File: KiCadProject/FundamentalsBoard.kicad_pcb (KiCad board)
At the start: 2 copper layers, 62 parts, among them P1 CONN_02X02, P10 CONN_02X02, P11 CONN_01X03, P12 CONN_01X03, P2 CONN_02X02, P3 USB_OTG, P4 CONN_02X02, P5 CONN_01X03, P6 CONN_02X02, P7 CONN_02X02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

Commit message: Initial layout
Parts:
- P1, P10, P2, P4, P6, P7, P8: footprint Pin_Headers:Pin_Header_Straight_2x02 -> TylerCustom:Pin_Header_Straight_2x02
- RV1, RV10, RV2, RV3, RV4, RV5, RV6, RV7, RV8, RV9: footprint SMD_Packages:POT_SMD -> TylerCustom:ST-4
- moved P3 116.6 mm to (83.2, 130.2), turned to 270 degrees
- moved RV9 90.9 mm to (176.5, 134.0), turned to 90 degrees
- moved RV10 76.9 mm to (152.4, 134.0), turned to 90 degrees
- moved P2 66.8 mm to (178.4, 112.4)
- moved C1 64.0 mm to (88.3, 130.2), turned to 90 degrees
- moved C2 62.4 mm to (90.2, 130.2), turned to 90 degrees
- moved RV3 59.2 mm to (97.2, 120.7), turned to 90 degrees
- moved P9 55.3 mm to (120.7, 131.4)
- moved C3 54.4 mm to (91.4, 111.1), turned to 180 degrees
- moved R8 51.9 mm to (94.6, 113.7), turned to 270 degrees
- moved R17 51.1 mm to (94.6, 89.5), turned to 270 degrees
- moved R7 50.9 mm to (94.6, 109.2), turned to 270 degrees
- moved U5 48.3 mm to (97.8, 88.3)
- moved R12 48.2 mm to (99.1, 115.6)
- moved Q1 47.3 mm to (99.1, 112.4), turned to 180 degrees
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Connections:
- C1 pad 2: CMirror_p -> VCC
- C2 pad 2: CMirror_p -> VCC
- P3 pad 1: CMirror_p -> VCC
- P6 pad 1: CMirror_p -> VCC
- P6 pad 2: CMirror_p -> VCC
- R10 pad 1: CMirror_p -> VCC
- R11 pad 1: Net-(R11-Pad1) -> VCC
- R7 pad 1: Net-(R11-Pad1) -> VCC
- RV1 pad 1: CMirror_p -> VCC
- RV5 pad 2: CMirror_p -> VCC
- U1 pad 5: CMirror_p -> VCC
- U2 pad 5: CMirror_p -> VCC
- U3 pad 5: CMirror_p -> VCC
- U4 pad 5: CMirror_p -> VCC
- U5 pad 5: CMirror_p -> VCC
- U6 pad 5: CMirror_p -> VCC
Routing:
- net GND: track 0.00 -> 56.4 mm, vias 0 -> 15
- net C_EmitterOut: track 0.00 -> 36.2 mm
- net VCC: track 0.00 -> 25.5 mm, vias 0 -> 5
- net C_EmitterIn: track 0.00 -> 19.4 mm
- net Diff_in: track 0.00 -> 18.4 mm
- net Diff_out: track 0.00 -> 17.5 mm
- net Net-(P5-Pad1): track 0.00 -> 17.3 mm
- net Amp_out: track 0.00 -> 15.6 mm
- net STrigger_out: track 0.00 -> 12.5 mm
- net Amp_in: track 0.00 -> 12.4 mm
- net Int_out: track 0.00 -> 11.8 mm
- net Net-(C5-Pad1): track 0.00 -> 11.4 mm
- net Net-(Q2-Pad1): track 0.00 -> 10.9 mm
- net Net-(C3-Pad1): track 0.00 -> 8.98 mm
- net STrigger_in: track 0.00 -> 8.59 mm
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- added copper zone on B.Cu, net GND
- added copper zone on F.Cu, net VCC
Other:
- board outline added: 111.8 x 71.1 mm
- board text added: "Amplifier"
- board text added: "Common Emitter"
- board text added: "Current Mirror"
- board text added: "Differentiator"
- board text added: "Extra 10k Pot"
- board text added: "Extra 5k Pot"
- board text added: "IN"
- board text added: "INPUT"
- board text added: "Integrator"
- board text added: "LEDs"
- board text added: "OUT"
- board text added: "OUT+"
- board text added: "OUT-"
- board text added: "OUTPUT"
- board text added: "Oscillator"
- board text added: "Schmitt Trigger"
- board text added: "V1"
- board text added: "V2"
- board text added: "VOUT"
- board text added: "Voltage Adder"

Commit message: Improved layout
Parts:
- added P13: CONN_02X02, TylerCustom:Pin_Header_Straight_2x02, F.Cu at (83.8, 139.7)
- added R23: 5k, Resistors_SMD:R_0603, F.Cu at (85.9, 117.6)
- added R24: 5k, Resistors_SMD:R_0603, F.Cu at (90.4, 141.0)
- R11: value 10k -> 5k
- R12, RV3: value 5k -> 10k
- moved R10 79.2 mm to (108.0, 123.8)
- moved R9 79.2 mm to (106.0, 117.5)
- moved RV4 79.2 mm to (108.6, 113.0)
- moved U3 79.2 mm to (108.0, 120.7)
- moved C4 79.2 mm to (103.5, 114.9)
- moved P5 79.2 mm to (114.9, 116.8)
- moved R6 79.2 mm to (104.8, 121.9)
- moved R13 79.2 mm to (109.9, 117.5)
- moved R15 51.9 mm to (88.3, 116.8)
- moved C5 51.9 mm to (90.8, 113.7)
- moved RV6 51.9 mm to (97.2, 118.7)
- moved U4 51.9 mm to (91.4, 116.8)
- moved P7 51.9 mm to (91.8, 123.5)
- moved C6 49.1 mm to (94.0, 140.3)
- moved P8 49.1 mm to (107.3, 136.5)
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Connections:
- net Net-(C3-Pad1) renamed /CE_base
- net Net-(P11-Pad1) renamed /10kpot_1
- net Net-(P11-Pad2) renamed /10kpot_2
- net Net-(P11-Pad3) renamed /10kpot_3
- net Net-(P12-Pad1) renamed /5kpot_1
- net Net-(P12-Pad2) renamed /5kpot_2
- net Net-(P12-Pad3) renamed /5kpot_3
- net Net-(P9-Pad1) renamed /LED1_in
- net Net-(P9-Pad2) renamed /LED2_in
- net Net-(P9-Pad3) renamed /LED3_in
- net Net-(Q2-Pad1) renamed /CM_baseCollector
- net Net-(Q2-Pad3) renamed /CM_emitterSet
- net Net-(Q3-Pad3) renamed /CM_emitterMirror
- Q1 pad 3: Net-(Q1-Pad3) -> /CE_emitter
- R12 pad 2: Net-(Q1-Pad3) -> VCC
- R15 pad 1: GND -> VCC
- R17 pad 1: GND -> VCC
- R21 pad 2: Net-(R21-Pad2) -> Net-(R12-Pad1)
- RV3 pad 2: Net-(R12-Pad1) -> /CE_emitter
- RV6 pad 2: Net-(C5-Pad1) -> Net-(RV6-Pad2)
- U6 pad 4: Net-(R21-Pad2) -> Net-(R12-Pad1)
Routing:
- net Vadd_out: track 5.62 -> 20.7 mm
- net Net-(P3-Pad6): track 0.00 -> 11.2 mm
- net GND: track 56.4 -> 66.9 mm
- net /5kpot_1: track 0.00 -> 9.92 mm
- net /10kpot_3: track 0.00 -> 9.92 mm
- net /10kpot_1: track 0.00 -> 9.92 mm
- net /5kpot_3: track 0.00 -> 9.92 mm
- net /CE_emitter: track 0.00 -> 9.77 mm
- net Net-(C5-Pad1): track 11.4 -> 7.40 mm
- net /5kpot_2: track 0.00 -> 3.35 mm
- net /10kpot_2: track 0.00 -> 3.35 mm
- net Net-(Q1-Pad3): track 2.78 -> 0.00 mm
- net Net-(R12-Pad1): track 6.99 -> 4.51 mm
- net Net-(R21-Pad2): track 2.16 -> 0.00 mm
- net Net-(R17-Pad2): track 2.86 -> 4.88 mm
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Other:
- board size 111.8 x 71.1 mm -> 71.8 x 64.1 mm
- board text added: "10k Pot"
- board text added: "5k Pot"
- board text added: "F=100Hz->inf"
- board text added: "G=0->2"
- board text added: "G=0.5-inf"
- board text added: "GND"
- board text added: "Range: 410 uA to 8.6 mA"
- board text added: "Sets Hysteresis"
- board text added: "Sets Q Point"
- board text added: "VCC"
- board text removed: "Extra 10k Pot"
- board text removed: "Extra 5k Pot"

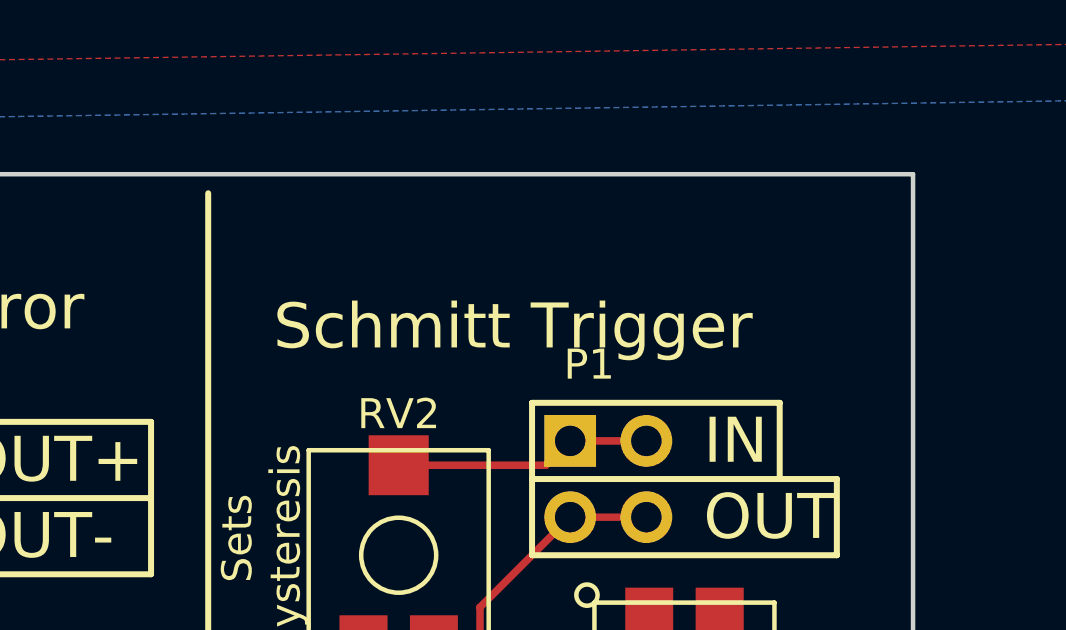
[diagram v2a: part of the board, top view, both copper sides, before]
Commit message: Final routing and Gerber export
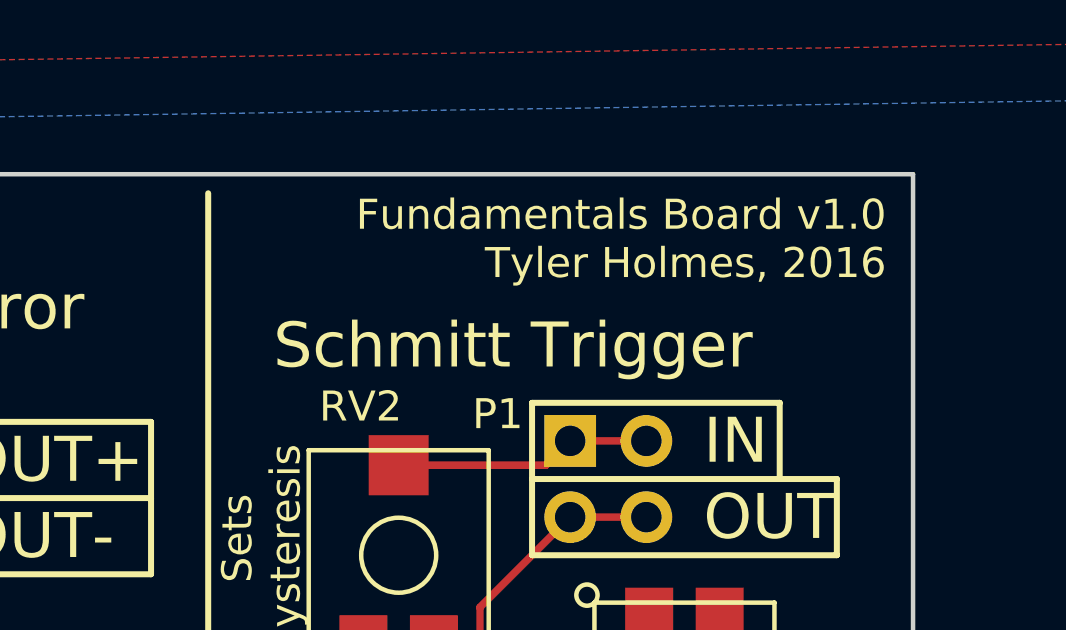
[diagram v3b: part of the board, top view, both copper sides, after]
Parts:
- R14, R16: value 500R -> 470R
- RV1, RV3, RV4, RV5, RV6, RV7, RV8, RV9: value 10k -> v10k
- RV10, RV2: value 5k -> v5k
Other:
- board text added: "Fundamentals Board v1.0 Tyler Holmes, 2016"
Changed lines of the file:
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@@
     (area 77.47 76.2 166.370001 149.225001)
     (thickness 1.6)
-    (drawings 123)
+    (drawings 124)
     (tracks 308)
     (zones 0)
@@
       (effects (font (size 1 1) (thickness 0.15)))
     )
-    (fp_text value 5k (at 0 0) (layer F.Fab)
+    (fp_text value v5k (at 0 0) (layer F.Fab)
       (effects (font (size 1 1) (thickness 0.15)))
     )
@@
       (effects (font (size 1 1) (thickness 0.15)))
     )
-    (fp_text value 10k (at 0 0) (layer F.Fab)
+    (fp_text value v10k (at 0 0) (layer F.Fab)
       (effects (font (size 1 1) (thickness 0.15)))
     )
@@
       (effects (font (size 1 1) (thickness 0.15)))
     )
-    (fp_text value 10k (at 0 0) (layer F.Fab)
+    (fp_text value v10k (at 0 0) (layer F.Fab)
       (effects (font (size 1 1) (thickness 0.15)))
     )
@@
       (effects (font (size 1 1) (thickness 0.15)))
     )
-    (fp_text value 10k (at 0 -4.75) (layer F.Fab) hide
+    (fp_text value v10k (at 0 -4.75) (layer F.Fab) hide
       (effects (font (size 1 1) (thickness 0.15)))
     )
@@
       (effects (font (size 1 1) (thickness 0.15)))
     )
-    (fp_text value 10k (at 0 0) (layer F.Fab)
+    (fp_text value v10k (at 0 0) (layer F.Fab)
       (effects (font (size 1 1) (thickness 0.15)))
     )
@@
       (effects (font (size 1 1) (thickness 0.15)))
     )
-    (fp_text value 10k (at 0 0) (layer F.Fab)
+    (fp_text value v10k (at 0 0) (layer F.Fab)
       (effects (font (size 1 1) (thickness 0.15)))
     )
@@
       (effects (font (size 1 1) (thickness 0.15)))
     )
-    (fp_text value 10k (at 0 0 270) (layer F.Fab)
+    (fp_text value v10k (at 0 0 270) (layer F.Fab)
       (effects (font (size 1 1) (thickness 0.15)))
     )
@@
       (effects (font (size 1 1) (thickness 0.15)))
     )
-    (fp_text value 10k (at 0 0 90) (layer F.Fab)
+    (fp_text value v10k (at 0 0 90) (layer F.Fab)
       (effects (font (size 1 1) (thickness 0.15)))
     )
@@
   (module TylerCustom:ST-4 (layer F.Cu)
     (at 135.89 93.345)
-    (fp_text reference RV2 (at 0 -4.699 180) (layer F.SilkS)
-      (effects (font (size 1 1) (thickness 0.15)))
-    )
-    (fp_text value 5k (at 0 0) (layer F.Fab)
+    (fp_text reference RV2 (at -1.27 -4.953 180) (layer F.SilkS)
+      (effects (font (size 1 1) (thickness 0.15)))
+    )
+    (fp_text value v5k (at 0 0) (layer F.Fab)
       (effects (font (size 1 1) (thickness 0.15)))
     )
@@
       (effects (font (size 1 1) (thickness 0.15)))
     )
-    (fp_text value 10k (at 0 0 180) (layer F.Fab)
+    (fp_text value v10k (at 0 0 180) (layer F.Fab)
       (effects (font (size 1 1) (thickness 0.15)))
     )
@@
       (effects (font (size 1 1) (thickness 0.15)))
     )
-    (fp_text value 500R (at 0 1.9 90) (layer F.Fab) hide
+    (fp_text value 470R (at 0 1.9 90) (layer F.Fab) hide
       (effects (font (size 1 1) (thickness 0.15)))
     )
@@
       (effects (font (size 1 1) (thickness 0.15)))
     )
-    (fp_text value 500R (at 0 1.9 90) (layer F.Fab) hide
+    (fp_text value 470R (at 0 1.9 90) (layer F.Fab) hide
       (effects (font (size 1 1) (thickness 0.15)))
     )
@@
     (descr "Through hole pin header")
     (tags "pin header")
-    (fp_text reference P1 (at 0.635 -2.54) (layer F.SilkS)
+    (fp_text reference P1 (at -2.413 -0.889) (layer F.SilkS)
       (effects (font (size 1 1) (thickness 0.15)))
     )
@@
       (rotate (xyz 0 0 90))
     )
+  )
+  (gr_text "Fundamentals Board v1.0\nTyler Holmes, 2016" (at 152.146 82.804) (layer F.SilkS)
+    (effects (font (size 1 1) (thickness 0.15)) (justify right))
   )
   (gr_line (start 82.55 144.272) (end 85.09 144.272) (layer F.SilkS) (width 0.2))
@@
     (effects (font (size 1.5 1.5) (thickness 0.3)) (justify right))
   )
-  (gr_text "Schmitt Trigger\n" (at 139.7 85.725) (layer F.SilkS)
+  (gr_text "Schmitt Trigger\n" (at 139.7 86.36) (layer F.SilkS)
     (effects (font (size 1.5 1.5) (thickness 0.3)))
   )

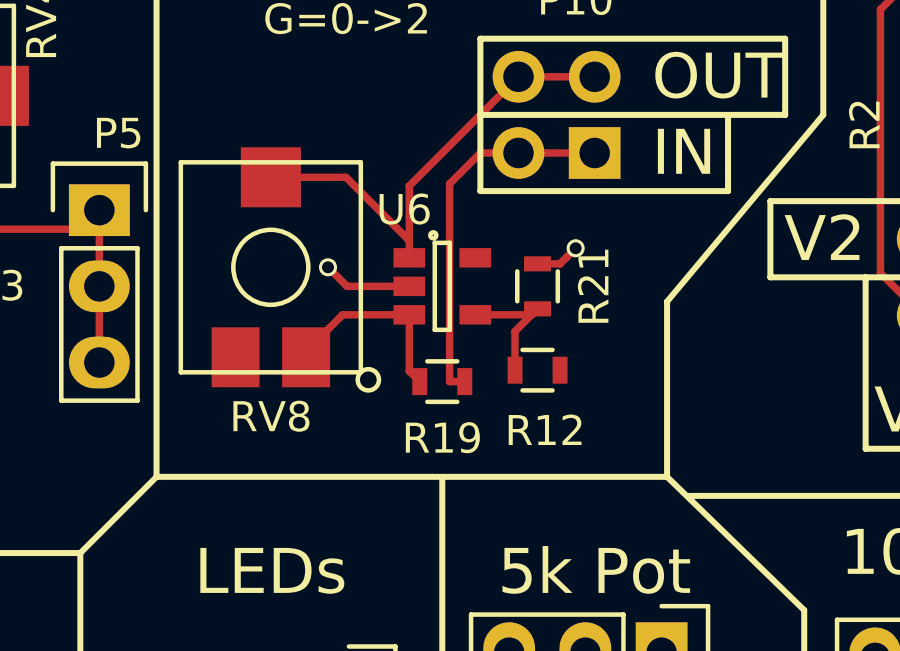
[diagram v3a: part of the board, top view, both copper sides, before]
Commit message: Corrected mistake in Amplifier feedback
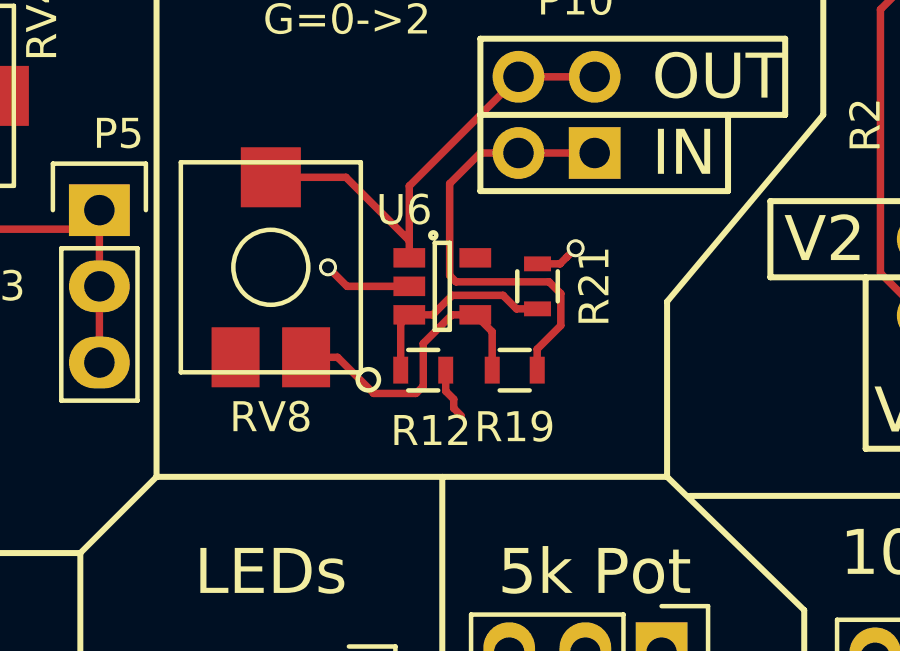
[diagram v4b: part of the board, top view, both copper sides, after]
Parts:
- moved R12 3.81 mm to (125.7, 122.2)
- moved R19 2.44 mm to (128.8, 122.2)
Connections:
- net Net-(C4-Pad2) renamed /osc_RCFeedback
- net Net-(C5-Pad1) renamed /int_VnFeedback
- net Net-(C6-Pad2) renamed /diff_VnFeedback
- net Net-(P5-Pad1) renamed /osc_schmittFeedback
- net Net-(R1-Pad1) renamed /Vp_Gnd
- net Net-(R10-Pad2) renamed /osc_bias
- net Net-(R13-Pad2) renamed /osc_VpIn
- net Net-(R15-Pad2) renamed /int_VpBias
- net Net-(R17-Pad2) renamed /diff_VpBias
- net Net-(R2-Pad1) renamed /Vadd_VnFeedback
- net Net-(R5-Pad2) renamed /schmitt_VpFeedback
- net Net-(RV1-Pad2) renamed /schmitt_bias
- R12 pad 1: Net-(R12-Pad1) -> /Amp_VpBias
- R19 pad 1: Net-(R19-Pad1) -> /amp_VnFeedback
- R21 pad 2: Net-(R12-Pad1) -> /Amp_VpBias
- RV8 pad 1: Net-(R19-Pad1) -> /amp_VnFeedback
- U6 pad 3: Net-(R19-Pad1) -> /Amp_VpBias
- U6 pad 4: Net-(R12-Pad1) -> /amp_VnFeedback
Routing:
- net /amp_VnFeedback: track 0.00 -> 10.3 mm
- net /Amp_VpBias: track 0.00 -> 6.69 mm
- net Net-(R19-Pad1): track 6.51 -> 0.00 mm
- net Net-(R12-Pad1): track 4.51 -> 0.00 mm
- net Amp_in: track 12.4 -> 15.2 mm
- net VCC: track 26.9 -> 28.7 mm

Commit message: Fixed version number
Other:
- board text added: "Fundamentals Board v1.1 Tyler Holmes, 2016"
- board text removed: "Fundamentals Board v1.0 Tyler Holmes, 2016"
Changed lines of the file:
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@@
     (links 131)
     (no_connects 0)
-    (area 81.204999 80.569999 153.110001 144.855001)
+    (area 77.47 76.2 166.370001 149.225001)
     (thickness 1.6)
     (drawings 124)
@@
     )
   )
-  (gr_text "Fundamentals Board v1.0\nTyler Holmes, 2016" (at 152.146 82.804) (layer F.SilkS)
+  (gr_text "Fundamentals Board v1.1\nTyler Holmes, 2016" (at 152.146 82.804) (layer F.SilkS)
     (effects (font (size 1 1) (thickness 0.15)) (justify right))
   )
